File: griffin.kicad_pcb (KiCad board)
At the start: 2 copper layers, 100 x 90 mm, 0 parts

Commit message: update
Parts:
- added C1: 104, Capacitor_SMD:C_0603_1608Metric, F.Cu at (135.0, 128.0)
- added C10: 105, Capacitor_SMD:C_0603_1608Metric, F.Cu at (131.0, 128.0)
- added C11: 104, Capacitor_SMD:C_0603_1608Metric, F.Cu at (174.0, 88.7)
- added C12: 104, Capacitor_SMD:C_0603_1608Metric, F.Cu at (139.0, 128.0)
- added C13: 104, Capacitor_SMD:C_0603_1608Metric, F.Cu at (119.0, 130.5)
- added C14: 104, Capacitor_SMD:C_0603_1608Metric, F.Cu at (123.0, 130.5)
- added C2: 104, Capacitor_SMD:C_0603_1608Metric, F.Cu at (184.2, 86.5)
- added C3: 15pF, Capacitor_SMD:C_0603_1608Metric, F.Cu at (184.2, 84.0)
- added C4: 15pF, Capacitor_SMD:C_0603_1608Metric, F.Cu at (160.0, 103.7)
- added C5: 104, Capacitor_SMD:C_0603_1608Metric, F.Cu at (160.0, 101.1)
- added C6: 104, Capacitor_SMD:C_0603_1608Metric, F.Cu at (123.0, 128.0)
- added C7: 22pF, Capacitor_SMD:C_0603_1608Metric, F.Cu at (135.0, 130.5)
- added C8: 22pF, Capacitor_SMD:C_0603_1608Metric, F.Cu at (119.0, 128.0)
- added C9: 104, Capacitor_SMD:C_0603_1608Metric, F.Cu at (127.0, 128.0)
- added D1: LED, LED_SMD:LED_0603_1608Metric, F.Cu at (160.1, 98.6)
- added D2: LED, LED_SMD:LED_0603_1608Metric, F.Cu at (104.2, 129.1)
- added F1: Fuse 0.75A, Fuse:Fuse_0805_2012Metric, F.Cu at (100.0, 129.3)
- added J1: USB_B_Micro, Connector_USB:USB_Micro-AB_Molex_47590-0001, F.Cu at (125.7, 56.2)
- added J2: Conn_02x03_Odd_Even, Connector_PinHeader_2.54mm:PinHeader_1x06_P2.54mm_Vertical, F.Cu at (165.0, 89.8)
- added J3: Conn_01x04, Connector_PinHeader_2.54mm:PinHeader_1x04_P2.54mm_Vertical, F.Cu at (169.6, 89.8)
- added J4: Conn_01x11, Connector_PinHeader_2.54mm:PinHeader_1x11_P2.54mm_Vertical, F.Cu at (155.7, 77.2)
- added J5: Conn_01x04, Connector_PinHeader_2.54mm:PinHeader_1x04_P2.54mm_Vertical, F.Cu at (151.0, 114.9)
- added J6: Conn_01x20, Connector_PinHeader_2.54mm:PinHeader_1x20_P2.54mm_Vertical, F.Cu at (100.1, 77.2)
- added J7: Conn_01x20, Connector_PinHeader_2.54mm:PinHeader_1x20_P2.54mm_Vertical, F.Cu at (104.7, 77.2)
- added J8: Conn_01x14, Connector_PinHeader_2.54mm:PinHeader_1x14_P2.54mm_Vertical, F.Cu at (151.0, 77.2)
- added J9: Conn_01x08, Connector_PinHeader_2.54mm:PinHeader_1x08_P2.54mm_Vertical, F.Cu at (160.3, 77.2)
- added R1: 1M, Resistor_SMD:R_0603_1608Metric, F.Cu at (127.0, 130.5)
- added R2: 10k, Resistor_SMD:R_0603_1608Metric, F.Cu at (178.0, 88.7)
- added R3: 10R, Resistor_SMD:R_0603_1608Metric, F.Cu at (174.0, 91.2)
- added R4: 10R, Resistor_SMD:R_0603_1608Metric, F.Cu at (178.0, 91.2)
- added R5: 1.5k, Resistor_SMD:R_0603_1608Metric, F.Cu at (139.0, 130.5)
- added R6: 1k, Resistor_SMD:R_0603_1608Metric, F.Cu at (131.0, 130.5)
- added R7: 1k, Resistor_SMD:R_0603_1608Metric, F.Cu at (169.3, 101.0)
- added R8: 10k, Resistor_SMD:R_0603_1608Metric, F.Cu at (174.0, 96.2)
- added R9: 10k, Resistor_SMD:R_0603_1608Metric, F.Cu at (174.0, 93.7)
- added SW1: SW_Push, Button_Switch_THT:SW_PUSH_6mm_H8.5mm, F.Cu at (122.0, 87.0)
- added SW2: SW_Push, Button_Switch_THT:SW_PUSH_6mm, F.Cu at (132.6, 87.0)
- added U1: STM32F103C8T6, lc_lib:LQFP-48_7X7X05P, F.Cu at (128.0, 105.0)
- added Y1: 32.768KHz, Crystal:Crystal_Round_D3.0mm_Vertical, F.Cu at (108.6, 129.2)
- added Y2: 8MHz, Crystal:Crystal_Round_D3.0mm_Vertical, F.Cu at (113.5, 129.2)

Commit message: update
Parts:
- added IC1: ME6211C33M5G-N, griffin:SOT95P270X145-5N, F.Cu at (125.9, 65.3)
- J2: footprint Connector_PinHeader_2.54mm:PinHeader_1x06_P2.54mm_Vertical -> Connector_PinSocket_2.54mm:PinSocket_1x06_P2.54mm_Vertical
- J3, J5: footprint Connector_PinHeader_2.54mm:PinHeader_1x04_P2.54mm_Vertical -> Connector_PinSocket_2.54mm:PinSocket_1x04_P2.54mm_Vertical
- J4: footprint Connector_PinHeader_2.54mm:PinHeader_1x11_P2.54mm_Vertical -> Connector_PinSocket_2.54mm:PinSocket_1x11_P2.54mm_Vertical
- J8: footprint Connector_PinHeader_2.54mm:PinHeader_1x14_P2.54mm_Vertical -> Connector_PinSocket_2.54mm:PinSocket_1x14_P2.54mm_Vertical
- J9: footprint Connector_PinHeader_2.54mm:PinHeader_1x08_P2.54mm_Vertical -> Connector_PinSocket_2.54mm:PinSocket_1x08_P2.54mm_Vertical
- SW1: footprint Button_Switch_THT:SW_PUSH_6mm_H8.5mm -> Button_Switch_THT:SW_MEC_5GTH9
- U1: value STM32F103C8T6 -> STM32F103C8Tx; footprint lc_lib:LQFP-48_7X7X05P -> Package_QFP:LQFP-48_7x7mm_P0.5mm
- Y2: footprint Crystal:Crystal_Round_D3.0mm_Vertical -> Crystal:Crystal_HC49-U_Vertical
- moved F1 63.2 mm to (125.0, 71.3)
- moved D2 63.2 mm to (129.2, 71.1)
- moved J8 49.5 mm to (101.6, 75.4)
- moved J5 49.4 mm to (101.6, 115.7)
- moved J9 40.9 mm to (149.5, 116.7)
- moved SW2 36.4 mm to (105.7, 62.4)
- moved Y1 36.2 mm to (125.4, 97.2)
- moved J7 33.7 mm to (138.4, 77.6)
- moved SW1 31.1 mm to (139.0, 61.0)
- moved J2 24.8 mm to (168.3, 114.3)
- moved U1 21.3 mm to (126.7, 83.7)
- moved C10 19.4 mm to (128.3, 108.8)
- moved C6 19.4 mm to (120.3, 108.8)
- moved C9 19.4 mm to (124.3, 108.8)
- moved C1 19.4 mm to (132.3, 108.8)
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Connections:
- C14 pad 1: (no net) -> /VBAT
- J3 pad 2: (no net) -> /PA14
- J3 pad 3: (no net) -> /PA13
- J4 pad 1: (no net) -> +5V
- J4 pad 10: (no net) -> /PB8
- J4 pad 11: (no net) -> /PB9
- J4 pad 2: (no net) -> GND
- J4 pad 3: (no net) -> GND
- J4 pad 6: (no net) -> /PB6
- J4 pad 7: (no net) -> /PA5
- J4 pad 8: (no net) -> /PA7
- J4 pad 9: (no net) -> /PB7
- J5 pad 1: (no net) -> +3V3
- J5 pad 2: (no net) -> GND
- J5 pad 3: (no net) -> /PA5
- J5 pad 4: (no net) -> /PA7
- J6 pad 1: (no net) -> GND
- J6 pad 10: (no net) -> /PA4
- J6 pad 11: (no net) -> /PA5
- J6 pad 12: (no net) -> /PA6
- J6 pad 13: (no net) -> /PA7
- J6 pad 14: (no net) -> /PB0
- J6 pad 15: (no net) -> /PB1
- J6 pad 16: (no net) -> /BOOT1
- J6 pad 17: (no net) -> /PB10
- J6 pad 18: (no net) -> /PB11
- J6 pad 19: (no net) -> /RESET
- J6 pad 2: (no net) -> +5V
- J6 pad 20: (no net) -> GND
- J6 pad 3: (no net) -> +3V3
- J6 pad 4: (no net) -> /VBAT
- J6 pad 5: (no net) -> /LED2
- J6 pad 6: (no net) -> /PA0
- J6 pad 7: (no net) -> /PA1
- J6 pad 8: (no net) -> /PA2
- J6 pad 9: (no net) -> /PA3
- J7 pad 1: (no net) -> +3V3
- J7 pad 10: (no net) -> /PB3
- J7 pad 11: (no net) -> /PA15
- J7 pad 12: (no net) -> /PA12
- J7 pad 13: (no net) -> /PA11
- J7 pad 14: (no net) -> /PA10
- J7 pad 15: (no net) -> /PA9
- J7 pad 16: (no net) -> /PA8
- J7 pad 17: (no net) -> /PB15
- J7 pad 18: (no net) -> /PB14
- J7 pad 19: (no net) -> /PB13
- J7 pad 2: (no net) -> +5V
- J7 pad 20: (no net) -> /PB12
- J7 pad 3: (no net) -> GND
- J7 pad 4: (no net) -> /PB9
- J7 pad 5: (no net) -> /PB8
- J7 pad 6: (no net) -> /PB7
- J7 pad 7: (no net) -> /PB6
- J7 pad 8: (no net) -> /PB5
- J7 pad 9: (no net) -> /PB4
- J8 pad 1: (no net) -> +5V
- J8 pad 10: (no net) -> /PB5
- J8 pad 11: (no net) -> /PA10
- J8 pad 12: (no net) -> /PA9
- J8 pad 13: (no net) -> /PA8
- J8 pad 14: (no net) -> /PA1
- J8 pad 2: (no net) -> GND
- J8 pad 3: (no net) -> /PB9
- J8 pad 4: (no net) -> /PB8
- J8 pad 5: (no net) -> /PB7
- J8 pad 6: (no net) -> /PA7
- J8 pad 7: (no net) -> /PA5
- J8 pad 8: (no net) -> /PB6
- J8 pad 9: (no net) -> /PA6
- J9 pad 1: (no net) -> GND
- J9 pad 2: (no net) -> +3V3
- J9 pad 3: (no net) -> /PA5
- J9 pad 4: (no net) -> /PA7
- J9 pad 5: (no net) -> /PB8
- J9 pad 6: (no net) -> /PB7
- J9 pad 7: (no net) -> /PB9
- J9 pad 8: (no net) -> /PB6
- R2 pad 1: (no net) -> /BOOT0
- R4 pad 1: (no net) -> /PA12
- R5 pad 1: (no net) -> /PA11
- R8 pad 2: (no net) -> /BOOT1
- U1 pad 1: (no net) -> /VBAT
- U1 pad 10: (no net) -> /PA0
- U1 pad 11: (no net) -> /PA1
- U1 pad 12: (no net) -> /PA2
- U1 pad 13: (no net) -> /PA3
- U1 pad 14: (no net) -> /PA4
- U1 pad 15: (no net) -> /PA5
- U1 pad 16: (no net) -> /PA5
- U1 pad 17: (no net) -> /PA6
- U1 pad 18: (no net) -> /PB0
- U1 pad 19: (no net) -> /PB1
- U1 pad 2: (no net) -> /LED2
- U1 pad 20: (no net) -> /BOOT1
- U1 pad 21: (no net) -> /PB10
- U1 pad 22: (no net) -> /PB11
- U1 pad 23: (no net) -> GND
- U1 pad 24: (no net) -> +3V3
- U1 pad 25: (no net) -> /PB12
- U1 pad 26: (no net) -> /PB13
- U1 pad 27: (no net) -> /PB14
- U1 pad 28: (no net) -> /PB15
- U1 pad 29: (no net) -> /PA7
- U1 pad 30: (no net) -> /PA8
- U1 pad 31: (no net) -> /PA9
- U1 pad 32: (no net) -> /PA11
- U1 pad 33: (no net) -> /PA12
- U1 pad 34: (no net) -> /PA13
- U1 pad 35: (no net) -> GND
- U1 pad 36: (no net) -> +3V3
- U1 pad 37: (no net) -> /PA14
- U1 pad 38: (no net) -> /PA15
- U1 pad 39: (no net) -> /PB3
- U1 pad 40: (no net) -> /PB4
- U1 pad 41: (no net) -> /PB5
- U1 pad 42: (no net) -> /PB6
- U1 pad 43: (no net) -> /PB7
- U1 pad 44: (no net) -> /BOOT0
- U1 pad 45: (no net) -> /PB8
- U1 pad 46: (no net) -> /PB9
- U1 pad 47: (no net) -> GND
- U1 pad 48: (no net) -> +3V3
- U1 pad 5: (no net) -> Net-(C8-Pad2)
- U1 pad 6: (no net) -> Net-(C7-Pad2)
- U1 pad 7: (no net) -> /RESET
- U1 pad 8: (no net) -> GND
- U1 pad 9: (no net) -> +3V3

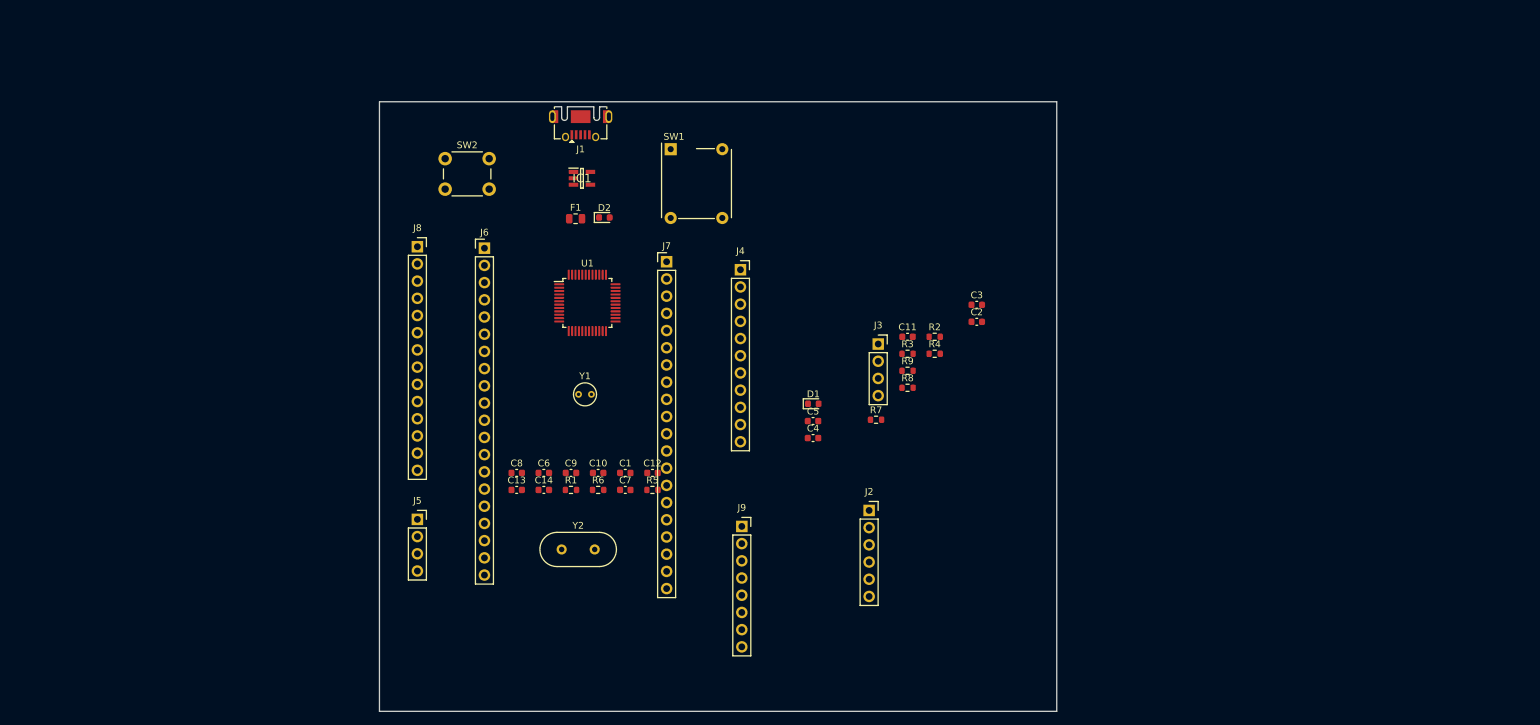
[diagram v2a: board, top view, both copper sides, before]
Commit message: resize height & width for PCB
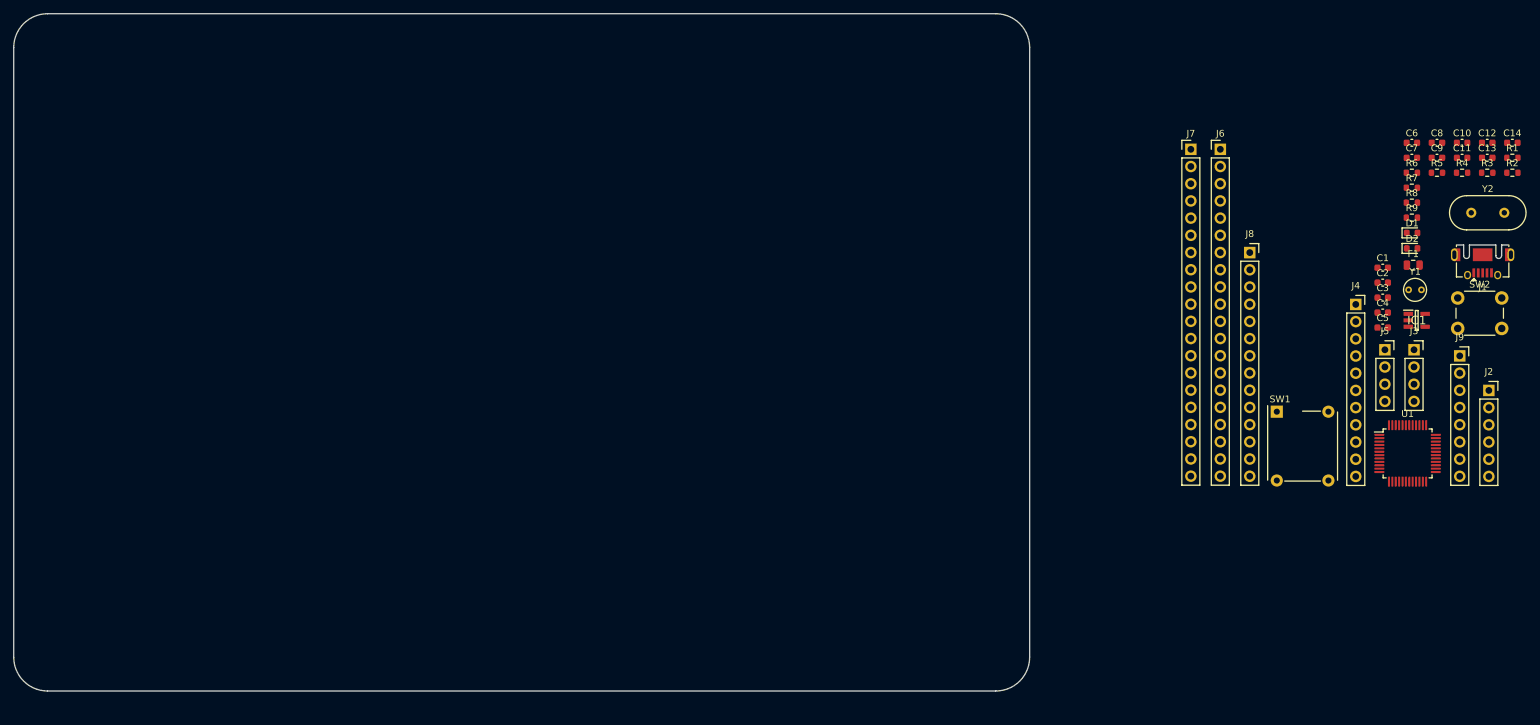
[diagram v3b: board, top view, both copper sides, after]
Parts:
- moved C14 151.9 mm to (263.3, 60.1)
- moved C13 151.5 mm to (259.6, 62.3)
- moved SW2 150.9 mm to (255.2, 83.0)
- moved R1 147.4 mm to (263.3, 62.3)
- moved J5 145.0 mm to (244.5, 90.6)
- moved C8 144.4 mm to (252.1, 60.1)
- moved Y2 143.2 mm to (257.2, 70.4)
- moved C6 137.1 mm to (248.4, 60.1)
- moved C10 136.6 mm to (255.9, 60.1)
- moved C9 136.1 mm to (252.1, 62.3)
- moved J1 134.7 mm to (258.9, 76.6)
- moved C12 132.5 mm to (259.6, 60.1)
- moved R6 128.9 mm to (248.4, 64.5)
- moved C7 126.1 mm to (248.4, 62.3)
- moved IC1 125.0 mm to (249.2, 86.3)
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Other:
- board size 100 x 90 mm -> 150 x 100 mm

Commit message: update schematic diagram
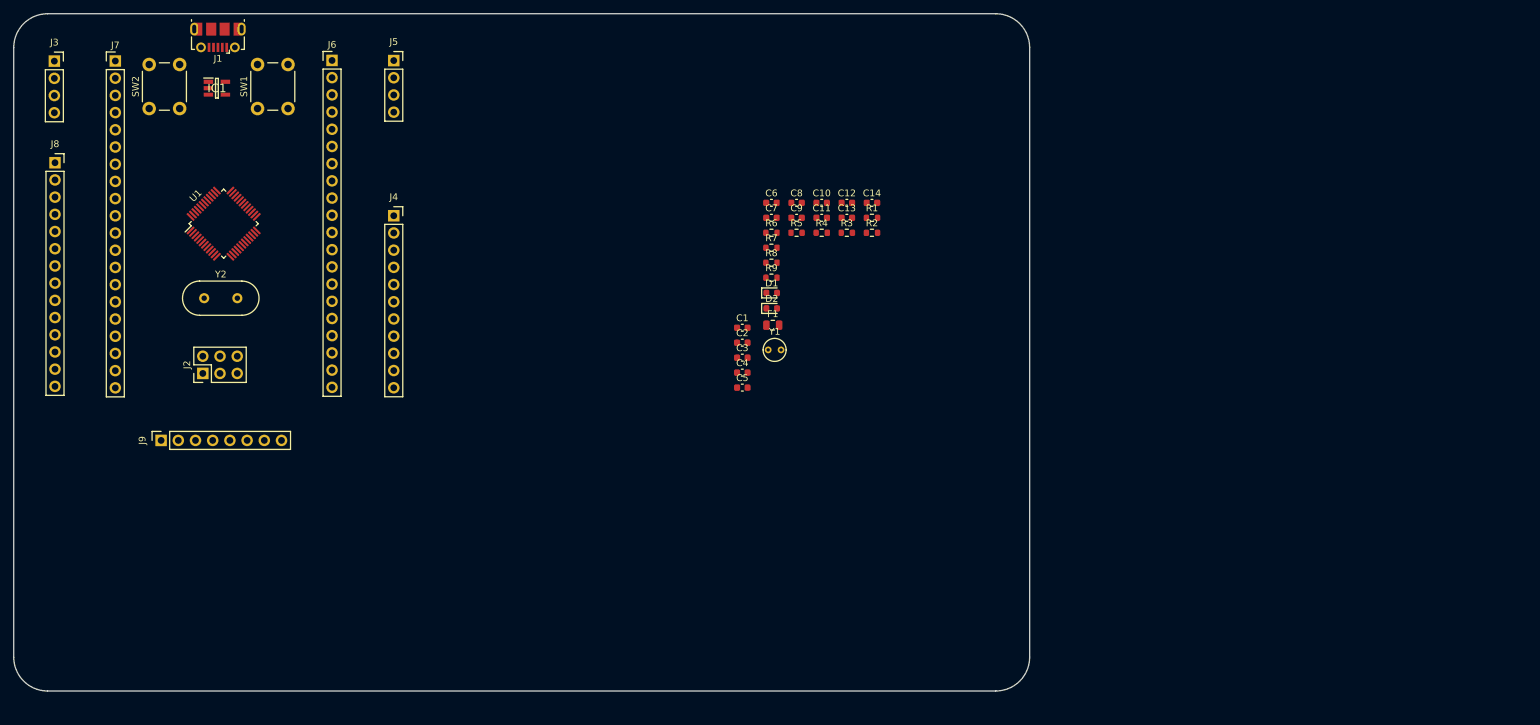
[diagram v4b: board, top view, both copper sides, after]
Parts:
- J1: footprint Connector_USB:USB_Micro-AB_Molex_47590-0001 -> Connector_USB:USB_Micro-B_Molex-105017-0001
- J2: footprint Connector_PinSocket_2.54mm:PinSocket_1x06_P2.54mm_Vertical -> Connector_PinHeader_2.54mm:PinHeader_2x03_P2.54mm_Vertical
- SW1: footprint Button_Switch_THT:SW_MEC_5GTH9 -> Button_Switch_THT:SW_PUSH_6mm
- Y2: footprint Crystal:Crystal_HC49-U_Vertical -> Crystal:Crystal_HC18-U_Vertical
- moved J3 205.2 mm to (48.0, 48.0)
- moved SW2 195.2 mm to (62.0, 55.0), turned to 90 degrees
- moved J9 192.1 mm to (63.8, 104.0), turned to 90 degrees
- moved J2 189.9 mm to (69.9, 94.1), turned to 90 degrees
- moved J1 189.5 mm to (72.2, 44.5)
- moved Y2 187.5 mm to (70.1, 83.0)
- moved IC1 180.4 mm to (72.0, 52.0)
- moved U1 178.1 mm to (73.0, 72.0), turned to 45 degrees
- moved J8 176.9 mm to (48.1, 63.0)
- moved J7 159.3 mm to (57.0, 48.0)
- moved SW1 157.0 mm to (78.0, 55.0), turned to 90 degrees
- moved J5 152.4 mm to (98.1, 47.9)
- moved J4 142.6 mm to (98.1, 70.8)
- moved J6 131.8 mm to (89.0, 47.9)
- moved C10 95.0 mm to (161.3, 68.9)
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
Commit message: update schematic diagram
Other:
- board text added: "test"
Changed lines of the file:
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@@
   (general
     (thickness 1.6)
-    (drawings 10)
+    (drawings 11)
     (tracks 0)
     (zones 0)
@@
     (aux_axis_origin 0 0)
     (grid_origin 192 141)
-    (visible_elements 7FFDFFFF)
+    (visible_elements 7FFFFFFF)
     (pcbplotparams
       (layerselection 0x010fc_ffffffff)
@@
     )
   )
+  (gr_text test (at 72 65) (layer F.SilkS)
+    (effects (font (size 1 1) (thickness 0.15)))
+  )
   (dimension 150 (width 0.15) (layer Dwgs.User)
